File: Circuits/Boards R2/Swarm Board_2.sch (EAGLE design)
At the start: 94 parts, among them CON1 ISP(2X3), CON2 MAIN_CONNECTOR, CON3 FTDI_3PIN, CON4 POWERJUMPER, T1 NPN2N2222, T10 TEFT4300, T11 NPN2N2222, T13 NPN2N2222, T14 NPN2N2222, T15 NPN2N2222, T16 NPN2N2222, T17 NPN2N2222, T18 NPN2N2222, T2 NPN2N2222, T3 NPN2N2222, T4 TEFT4300, T5 TEFT4300, T6 TEFT4300, T7 TEFT4300, T8 TEFT4300, T9 TEFT4300, U1 ATMEGA324P, U2 MCP73833

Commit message: updated R2 board
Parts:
- CON4: value POWERJUMPER -> HEADER_3X1; device Mechanical:POWERJUMPER -> Mechanical:HEADER_3X1
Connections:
- net +VBAT: now also CON4.2; no longer CON4.1
- net N$29: now also CON4.1; no longer CON4.2
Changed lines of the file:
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@@
 <?xml version="1.0" encoding="utf-8"?>
 <!DOCTYPE eagle SYSTEM "eagle.dtd">
-<eagle version="6.2">
+<eagle version="6.3">
 <drawing>
 <settings>
@@
 <part name="B1" library="Passive" deviceset="PIEZOBUZZER" device="PTH"/>
 <part name="P+4" library="Supply" deviceset="+3V" device=""/>
-<part name="CON4" library="Mechanical" deviceset="POWERJUMPER" device=""/>
+<part name="CON4" library="Mechanical" deviceset="HEADER_3X1" device=""/>
 <part name="P+16" library="Supply" deviceset="+VBAT" device=""/>
 </parts>
@@
 <instance part="B1" gate="G$1" x="-119.38" y="35.56"/>
 <instance part="P+4" gate="1" x="-71.12" y="7.62" rot="R270"/>
-<instance part="CON4" gate="G$1" x="73.66" y="-109.22"/>
-<instance part="P+16" gate="G$1" x="58.42" y="-127" rot="R90"/>
+<instance part="CON4" gate="G$1" x="38.1" y="-129.54" rot="R180"/>
+<instance part="P+16" gate="G$1" x="53.34" y="-129.54" rot="R270"/>
 </instances>
 <busses>
@@
 </segment>
 <segment>
-<pinref part="CON4" gate="G$1" pin="1"/>
-<wire x1="66.04" y1="-109.22" x2="66.04" y2="-127" width="0.1524" layer="91"/>
-<wire x1="66.04" y1="-127" x2="58.42" y2="-127" width="0.1524" layer="91"/>
+<pinref part="CON4" gate="G$1" pin="2"/>
+<wire x1="43.18" y1="-129.54" x2="53.34" y2="-129.54" width="0.1524" layer="91"/>
 <pinref part="P+16" gate="G$1" pin="+VBAT"/>
 </segment>
@@
 <segment>
 <pinref part="CON2" gate="G$1" pin="7"/>
-<pinref part="CON4" gate="G$1" pin="2"/>
-<wire x1="101.6" y1="-109.22" x2="86.36" y2="-109.22" width="0.1524" layer="91"/>
-</segment>
-</net>
+<wire x1="101.6" y1="-109.22" x2="66.04" y2="-109.22" width="0.1524" layer="91"/>
+<wire x1="66.04" y1="-109.22" x2="66.04" y2="-132.08" width="0.1524" layer="91"/>
+<pinref part="CON4" gate="G$1" pin="1"/>
+<wire x1="66.04" y1="-132.08" x2="43.18" y2="-132.08" width="0.1524" layer="91"/>
+</segment>
+</net>

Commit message: 
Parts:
- removed LED8: red, Passive:LED0603
- removed LED9: green, Passive:LED0603
- removed R25, R26: 750, Passive:RES0603
- added LED10: SMD_RGB, Passive:SMD_RGB
- added R3: 180, Passive:RES0603
- added R4, R5: 70, Passive:RES0603
- R10, R11, R12, R13, R14, R15: value (none) -> 100
- R17, R18, R19, R20, R21, R24, R27: value (none) -> 10k
- R22: value (none) -> 15
- R36, R37, R38, R39, R40, R41: value (none) -> 4.7k
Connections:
- net N$2 renamed MOSI
- net N$5 renamed SCK
- net N$6 renamed RESET
- removed net N$20: LED8.C, R25.2
- removed net N$21: LED9.C, R26.2
- removed net N$3: CON1.MISO, U1.PB6(PCINT14/MISO)
- new net MISO: CON1.MISO, R3.1, U1.PB6(PCINT14/MISO)
- new net N$30: LED10.REDCATHODE, R3.2
- new net N$31: LED10.BLUECATHODE, R4.2
- new net N$32: LED10.GREENCATHODE, R5.2
- net +VRAW: now also LED10.COMMONANODE
- net GND: no longer R25.1, R26.1
- net LED1: now also R4.1; no longer LED8.A
- net LED2: now also R5.1; no longer LED9.A
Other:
- moved on the sheet: ANT1, ANT2, ANT3

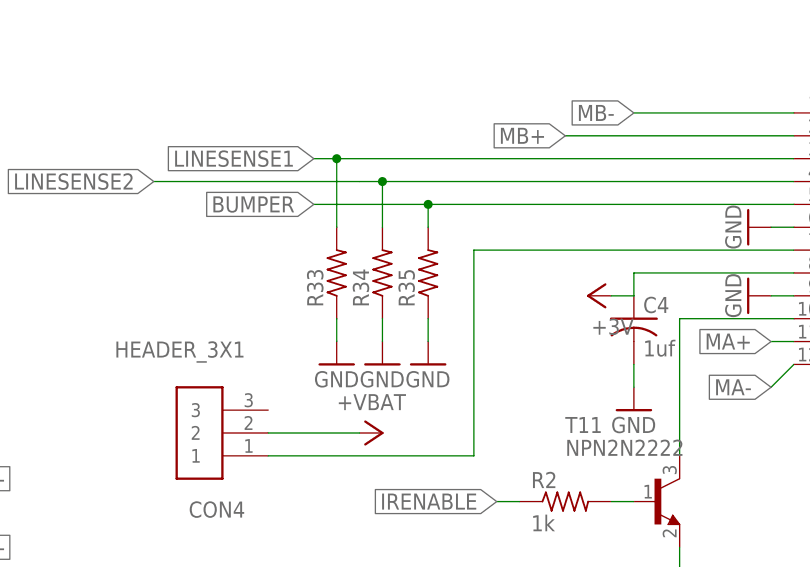
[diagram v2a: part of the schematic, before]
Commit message: 
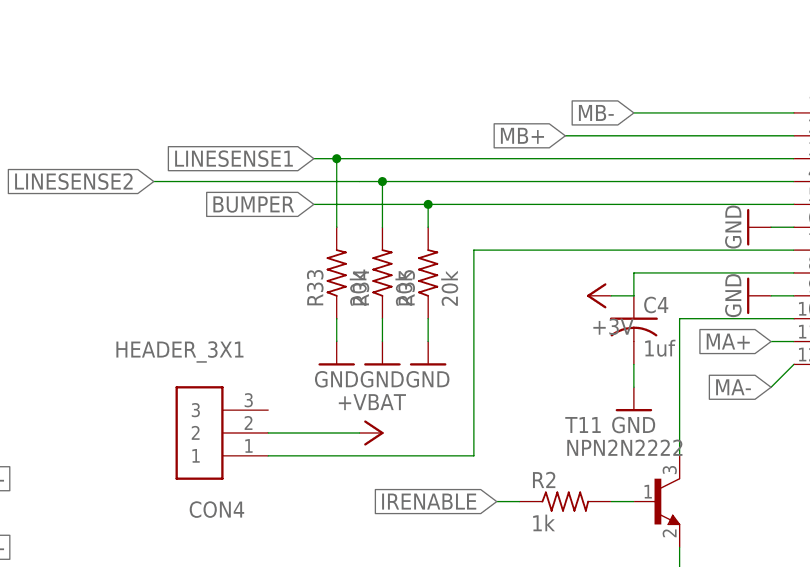
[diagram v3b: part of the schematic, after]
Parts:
- R33, R34, R35: value (none) -> 20k
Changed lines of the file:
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@@
 <part name="GND19" library="Supply" deviceset="GND" device=""/>
 <part name="P+17" library="Supply" deviceset="+3V" device=""/>
-<part name="R33" library="Passive" deviceset="RES" device="0603"/>
-<part name="R34" library="Passive" deviceset="RES" device="0603"/>
-<part name="R35" library="Passive" deviceset="RES" device="0603"/>
+<part name="R33" library="Passive" deviceset="RES" device="0603" value="20k"/>
+<part name="R34" library="Passive" deviceset="RES" device="0603" value="20k"/>
+<part name="R35" library="Passive" deviceset="RES" device="0603" value="20k"/>
 <part name="GND23" library="Supply" deviceset="GND" device=""/>
 <part name="GND24" library="Supply" deviceset="GND" device=""/>

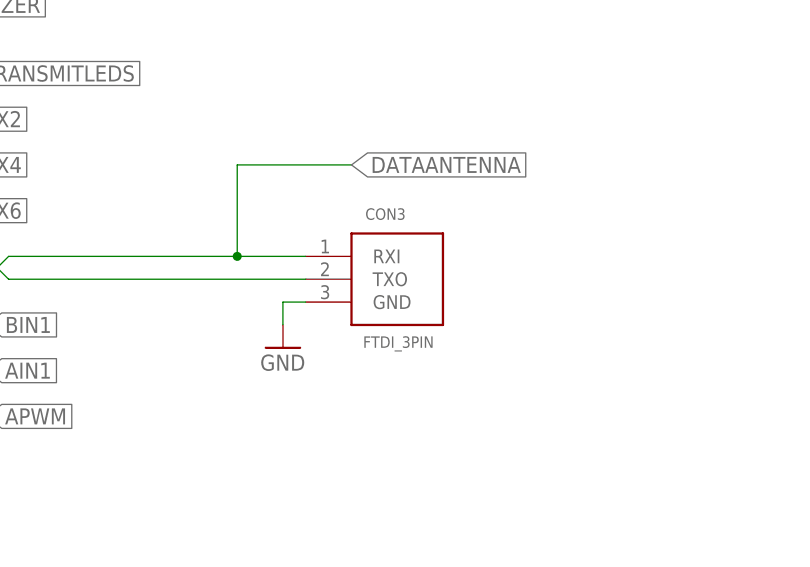
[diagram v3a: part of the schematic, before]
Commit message: fixed led on swarm board
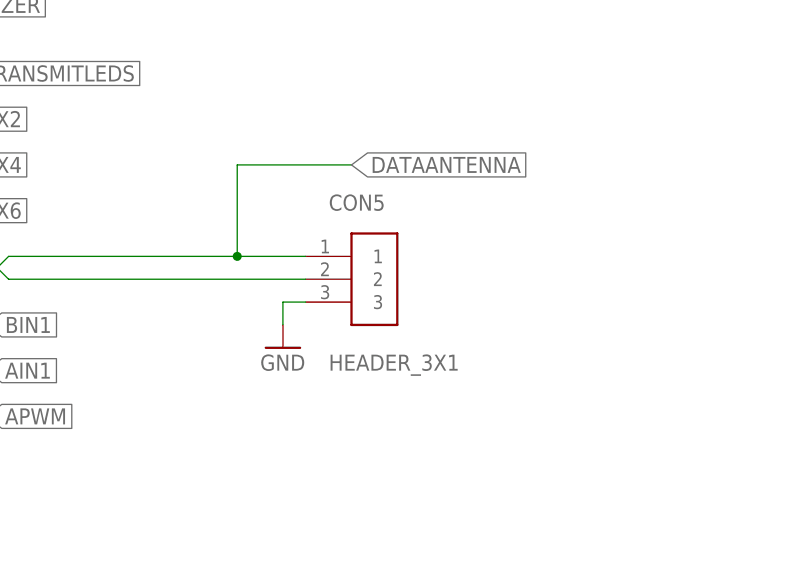
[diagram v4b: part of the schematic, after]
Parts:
- removed CON3: FTDI_3PIN, Mechanical:FTDI_3PIN
- added CON5: HEADER_3X1, Mechanical:HEADER_3X1
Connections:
- net DATAANTENNA: now also CON5.1; no longer CON3.RXI
- net GND: now also CON5.3; no longer CON3.GND
- net N$8: now also CON5.2; no longer CON3.TXO
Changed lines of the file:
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@@
 <?xml version="1.0" encoding="utf-8"?>
 <!DOCTYPE eagle SYSTEM "eagle.dtd">
-<eagle version="6.3">
+<eagle version="6.2">
 <drawing>
 <settings>
@@
 <part name="R28" library="Passive" deviceset="RES" device="0603" value="1k"/>
 <part name="CON2" library="Mechanical" deviceset="MAIN_CONNECTOR" device=""/>
-<part name="CON3" library="Mechanical" deviceset="FTDI_3PIN" device=""/>
 <part name="P+15" library="Supply" deviceset="+VCHG" device=""/>
 <part name="GND18" library="Supply" deviceset="GND" device=""/>
@@
 <part name="R4" library="Passive" deviceset="RES" device="0603" value="70"/>
 <part name="R5" library="Passive" deviceset="RES" device="0603" value="70"/>
+<part name="CON5" library="Mechanical" deviceset="HEADER_3X1" device=""/>
 </parts>
 <sheets>
@@
 <instance part="R28" gate="G$1" x="-144.78" y="20.32"/>
 <instance part="CON2" gate="G$1" x="114.3" y="-106.68"/>
-<instance part="CON3" gate="G$1" x="99.06" y="-25.4"/>
 <instance part="P+15" gate="G$1" x="-223.52" y="-20.32" rot="R270"/>
 <instance part="GND18" gate="1" x="-220.98" y="-45.72" rot="R90"/>
@@
 <instance part="R4" gate="G$1" x="-132.08" y="-43.18" rot="R90"/>
 <instance part="R5" gate="G$1" x="-124.46" y="-43.18" rot="R90"/>
+<instance part="CON5" gate="G$1" x="93.98" y="-25.4"/>
 </instances>
 <busses>
@@
 <wire x1="86.36" y1="-27.94" x2="86.36" y2="-30.48" width="0.1524" layer="91"/>
 <pinref part="GND5" gate="1" pin="GND"/>
-<pinref part="CON3" gate="G$1" pin="GND"/>
+<pinref part="CON5" gate="G$1" pin="3"/>
 </segment>
 <segment>
@@
 <pinref part="U1" gate="G$1" pin="PD1(PCINT25/TXD0)"/>
 <wire x1="53.34" y1="-25.4" x2="30.48" y2="-25.4" width="0.1524" layer="91"/>
-<pinref part="CON3" gate="G$1" pin="RXI"/>
 <wire x1="81.28" y1="-22.86" x2="81.28" y2="-12.7" width="0.1524" layer="91"/>
 <wire x1="81.28" y1="-12.7" x2="93.98" y2="-12.7" width="0.1524" layer="91"/>
 <label x="93.98" y="-12.7" size="1.778" layer="91" xref="yes"/>
 <junction x="81.28" y="-22.86"/>
+<pinref part="CON5" gate="G$1" pin="1"/>
 </segment>
 <segment>
@@
 <wire x1="53.34" y1="-22.86" x2="55.88" y2="-25.4" width="0.1524" layer="91"/>
 <wire x1="55.88" y1="-25.4" x2="88.9" y2="-25.4" width="0.1524" layer="91"/>
-<pinref part="CON3" gate="G$1" pin="TXO"/>
-</segment>
-</net>
+<pinref part="CON5" gate="G$1" pin="2"/>
+</segment>
+</net>

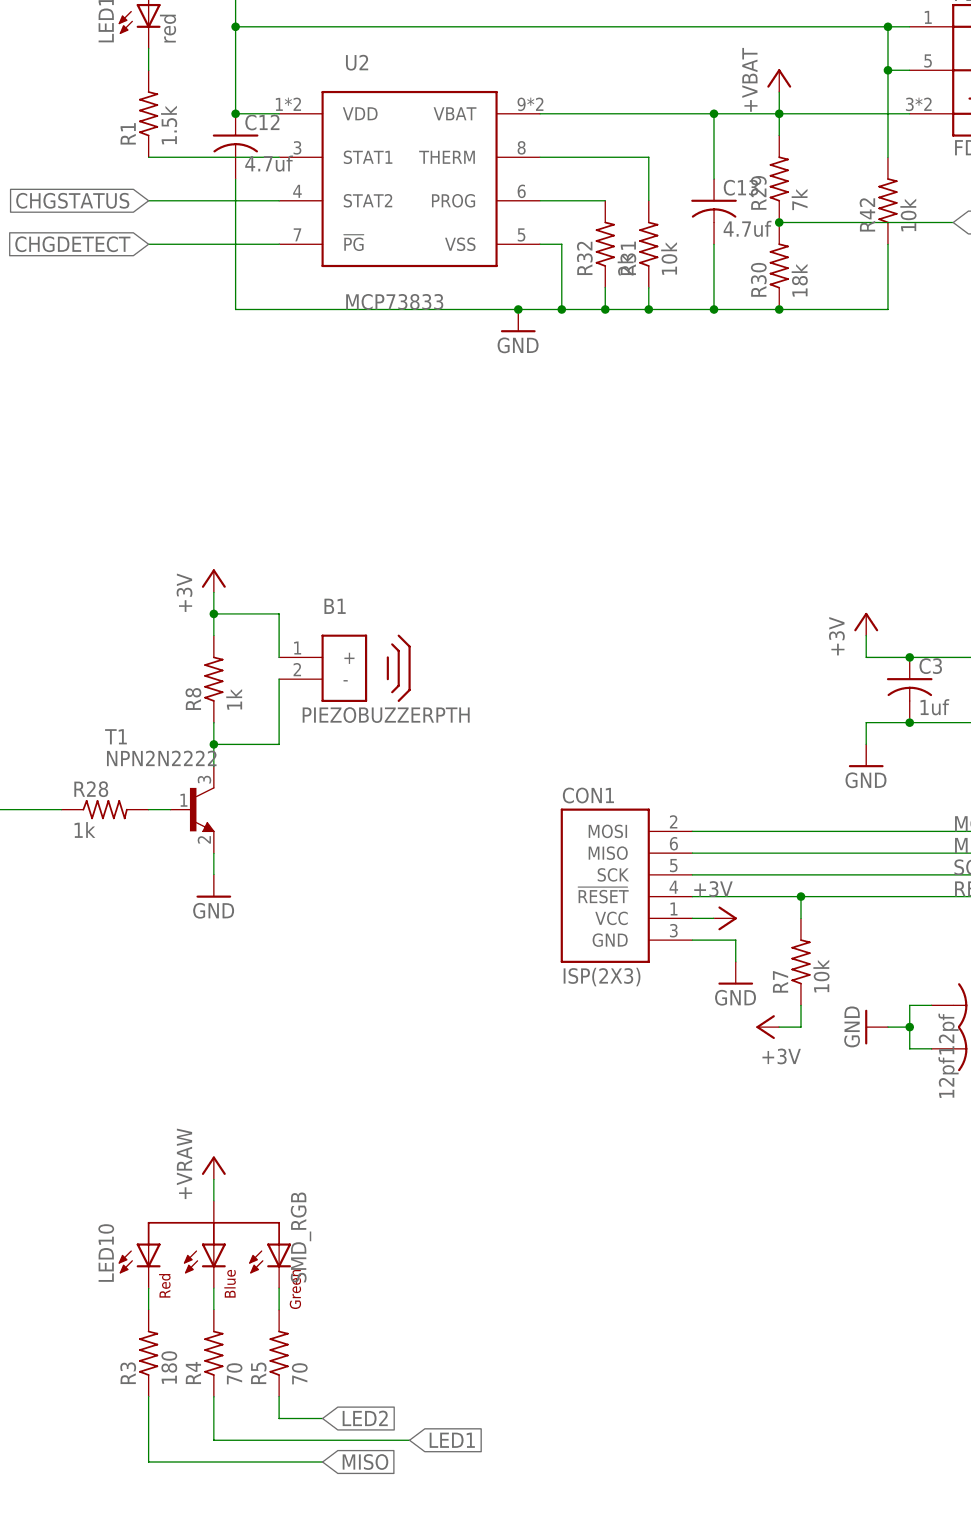
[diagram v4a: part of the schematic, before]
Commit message: slight updates to part values to account for availibility
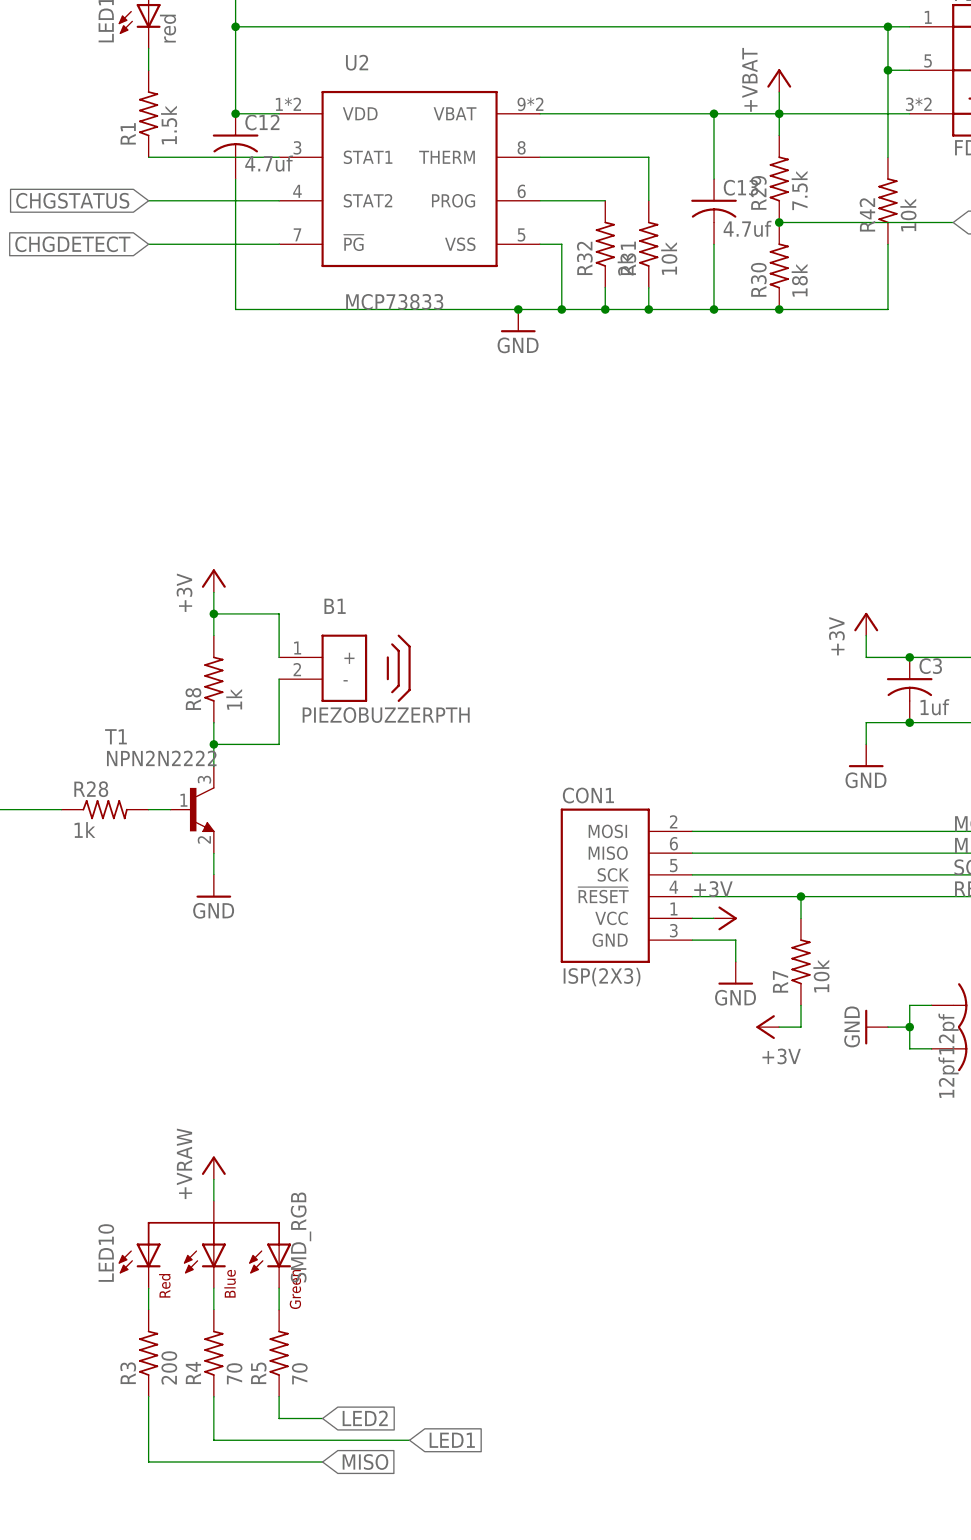
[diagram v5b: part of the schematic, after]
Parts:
- R29: value 7k -> 7.5k
- R3: value 180 -> 200
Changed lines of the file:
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@@
 <part name="P+3" library="Supply" deviceset="+3V" device=""/>
 <part name="U2" library="PowerIC" deviceset="MCP73833" device=""/>
-<part name="R29" library="Passive" deviceset="RES" device="0603" value="7k"/>
+<part name="R29" library="Passive" deviceset="RES" device="0603" value="7.5k"/>
 <part name="R30" library="Passive" deviceset="RES" device="0603" value="18k"/>
 <part name="R31" library="Passive" deviceset="RES" device="0603" value="10k"/>
@@
 <part name="LED10" library="Passive" deviceset="SMD_RGB" device=""/>
 <part name="P+20" library="Supply" deviceset="+VRAW" device=""/>
-<part name="R3" library="Passive" deviceset="RES" device="0603" value="180"/>
+<part name="R3" library="Passive" deviceset="RES" device="0603" value="200"/>
 <part name="R4" library="Passive" deviceset="RES" device="0603" value="70"/>
 <part name="R5" library="Passive" deviceset="RES" device="0603" value="70"/>
